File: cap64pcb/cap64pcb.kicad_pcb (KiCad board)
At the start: 2 copper layers, 91.6 x 8 mm, 29 parts, among them J1 SM05B_SURS_TF, Q1 BSS138, Q2 BSS138, U1 MPR121QR2, U2 SPX3819M5-L-3-3

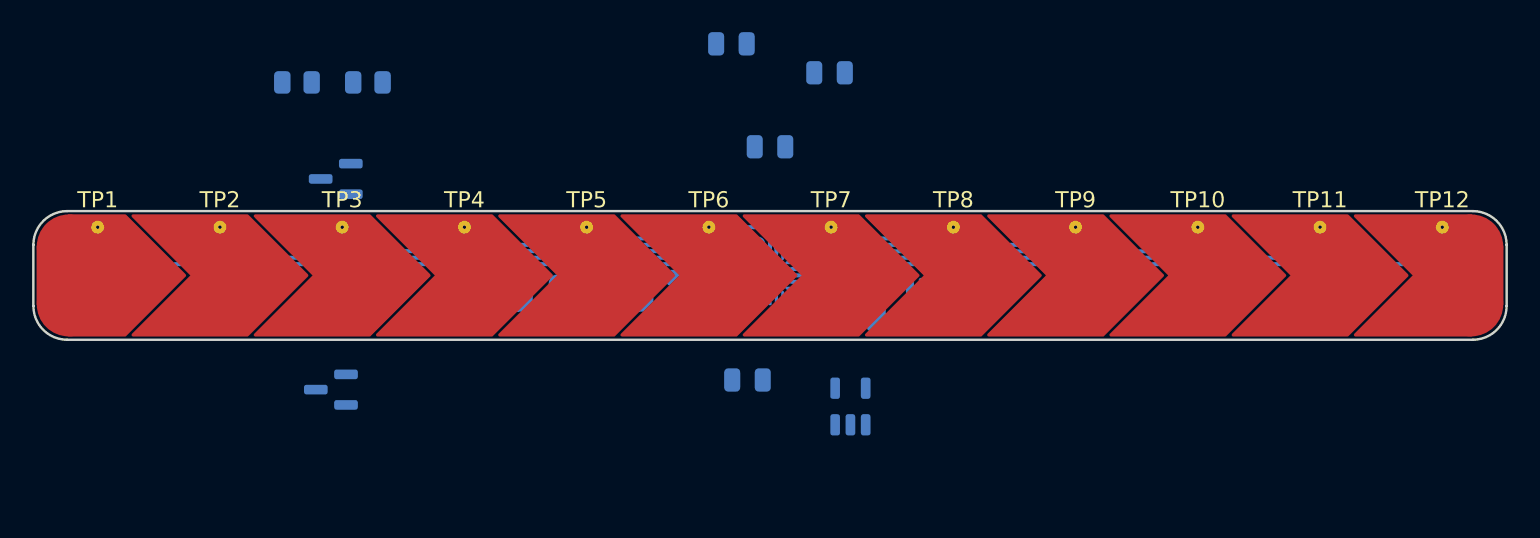
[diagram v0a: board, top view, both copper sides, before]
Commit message: updated sch and pcb with taller pads
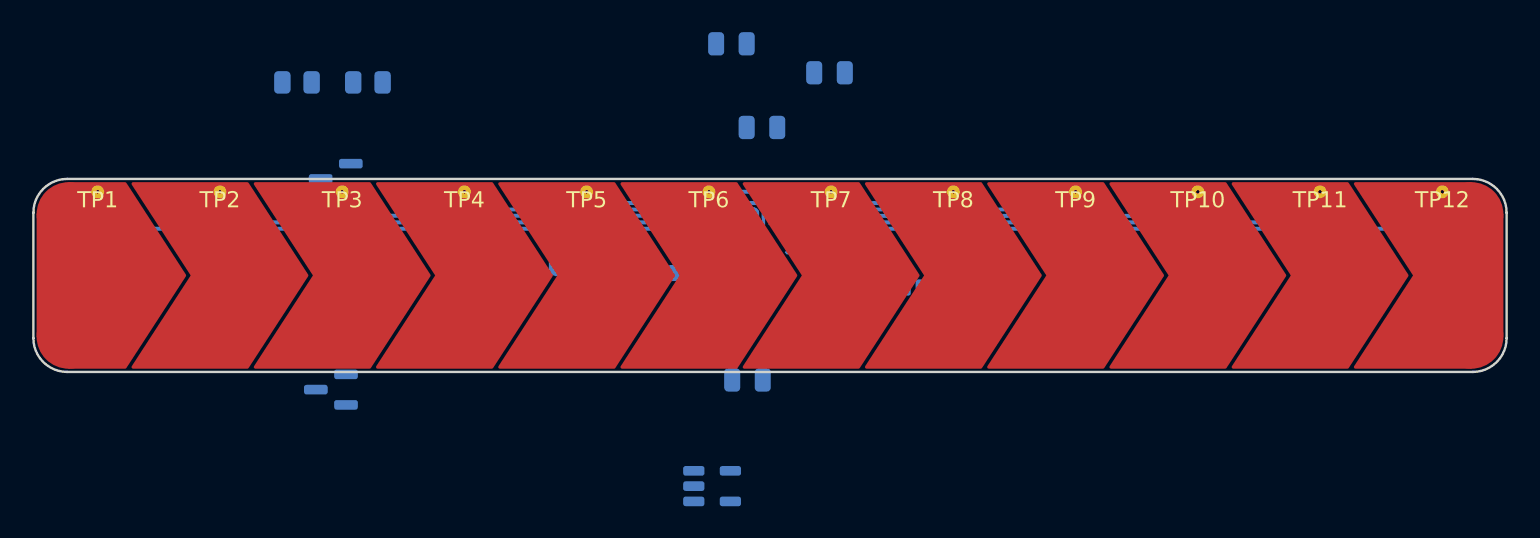
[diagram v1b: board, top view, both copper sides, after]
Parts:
- TP1: footprint cap_pads:CAPPAD_7.6x7.6_Chevron_1_TopPTH -> cap_pads:CAPPADS_7.6x11.6_Chevron_1
- TP10, TP11, TP2, TP3, TP4, TP5, TP6, TP7, TP8, TP9: footprint cap_pads:CAPPAD_7.6x7.6_Chevron_2_TopPTH -> cap_pads:CAPPADS_7.6x11.6_Chevron_2
- TP12: footprint cap_pads:CAPPAD_7.6x7.6_Chevron_3_TopPTH -> cap_pads:CAPPADS_7.6x11.6_Chevron_3
- moved U2 9.92 mm to (76.4, 58.1), turned to 0 degrees
- moved J1 2.42 mm to (88.5, 44.6), turned to 0 degrees
- moved C5 2.20 mm to (74.3, 43.9)
- moved JP1 2.20 mm to (69.5, 43.9)
- moved JP2 2.20 mm to (67.0, 43.9)
- moved JP3 2.20 mm to (64.5, 43.9)
- moved JP4 2.20 mm to (72.0, 43.9)
- moved R1 2.20 mm to (76.3, 43.9)
- moved U1 2.20 mm to (80.0, 42.8)
- moved C2 1.30 mm to (79.5, 35.8)
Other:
- board size 91.6 x 8 mm -> 91.6 x 12 mm

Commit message: shrunk pad radii by 0.01mm
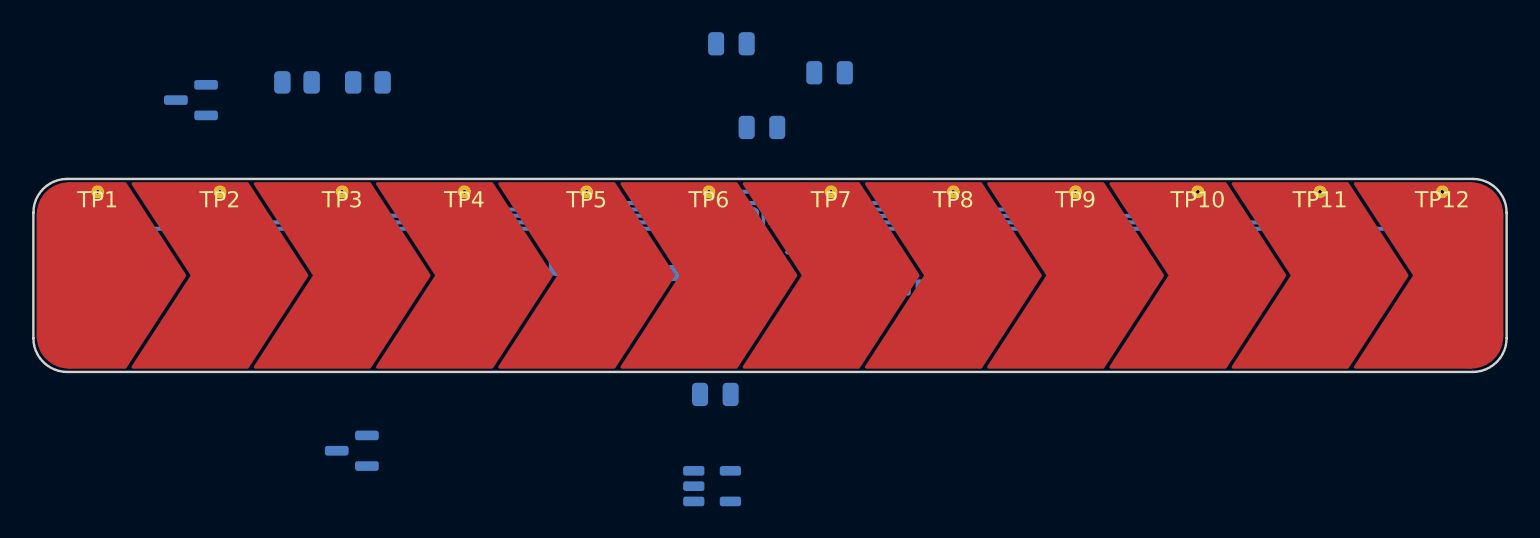
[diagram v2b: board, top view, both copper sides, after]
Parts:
- moved Q2 10.2 mm to (44.0, 34.1)
- moved Q1 4.02 mm to (54.0, 55.9)
- moved C4 2.19 mm to (76.6, 52.4)
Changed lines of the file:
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@@
             (xy -3.7 -3.8)
           ) (width 0.2) (fill yes))
-            (gr_circle (center -1.8 -3.8) (end 0.1 -3.8) (width 0.2) (fill yes))
-            (gr_circle (center -1.8 3.8) (end 0.1 3.8) (width 0.2) (fill yes))
+            (gr_circle (center -1.8 -3.8) (end 0.09 -3.8) (width 0.2) (fill yes))
+            (gr_circle (center -1.8 3.8) (end 0.09 3.8) (width 0.2) (fill yes))
       ))
     (pad "1" thru_hole circle (at 0 -5.2) (size 0.8 0.8) (drill 0.2) (layers *.Cu)
@@
             (xy -1.7 0)
           ) (width 0.2) (fill yes))
-            (gr_circle (center 1.8 3.8) (end 3.7 3.8) (width 0.2) (fill yes))
-            (gr_circle (center 1.8 -3.8) (end 3.7 -3.8) (width 0.2) (fill yes))
+            (gr_circle (center 1.8 3.8) (end 3.69 3.8) (width 0.2) (fill yes))
+            (gr_circle (center 1.8 -3.8) (end 3.69 -3.8) (width 0.2) (fill yes))
       ))
     (pad "1" thru_hole circle (at 0 -5.2) (size 0.8 0.8) (drill 0.2) (layers *.Cu)
@@
   )
   (footprint "Capacitor_SMD:C_0805_2012Metric" (layer "B.Cu")
-    (at 78.6 51.5 180)
+    (at 76.6 52.4 180)
     (descr "Capacitor SMD 0805 (2012 Metric), square (rectangular) end terminal, IPC_7351 nominal, (Body size source: IPC-SM-782 page 76, https://www.pcb-3d.com/wordpress/wp-content/uploads/ipc-sm-782a_amendment_1_and_2.pdf, https://docs.google.com/spreadsheets/d/1BsfQQcO9C6DZCsRaXUlFlo91Tg2WpOkGARC1WS5S8t0/edit?usp=sharing), generated with kicad-footprint-generator")
     (tags "capacitor")
@@
   )
   (footprint "Package_TO_SOT_SMD:SOT-23" (layer "B.Cu")
-    (at 52.7 52.1 180)
+    (at 54 55.9 180)
     (descr "SOT, 3 Pin (https://www.jedec.org/system/files/docs/to-236h.pdf variant AB), generated with kicad-footprint-generator ipc_gullwing_generator.py")
     (tags "SOT TO_SOT_SMD")
@@
   )
   (footprint "Package_TO_SOT_SMD:SOT-23" (layer "B.Cu")
-    (at 53 39 180)
+    (at 44 34.1 180)
     (descr "SOT, 3 Pin (https://www.jedec.org/system/files/docs/to-236h.pdf variant AB), generated with kicad-footprint-generator ipc_gullwing_generator.py")
     (tags "SOT TO_SOT_SMD")

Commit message: prepping silks
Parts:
- U2: value SPX3819M5-L-3-3 -> SPX3819M5-L-3.3
- moved C2 17.7 mm to (83.6, 53.0)
- moved JP1 15.0 mm to (62.8, 57.3), turned to -90 degrees
- moved JP3 13.1 mm to (71.0, 55.3), turned to -90 degrees
- moved JP2 12.5 mm to (67.4, 56.4), turned to -90 degrees
- moved U2 12.0 mm to (83.4, 48.3)
- moved C1 11.9 mm to (83.9, 44.3)
- moved JP4 1.70 mm to (70.3, 43.8)
- moved C5 1.70 mm to (72.6, 43.9)
- moved J1 1.26 mm to (89.7, 44.2)
- moved R1 1.06 mm to (75.6, 43.1), turned to 180 degrees
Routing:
- net GND: track 0.00 -> 9.16 mm

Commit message: arranging components
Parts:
- moved Q2 42.6 mm to (84.6, 47.0), turned to 0 degrees
- moved Q1 26.9 mm to (79.8, 48.4), turned to 0 degrees
- moved C1 7.92 mm to (91.0, 47.8)
- moved U2 7.65 mm to (90.7, 50.6), turned to 180 degrees
- moved J1 4.10 mm to (93.8, 44.1)
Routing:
- net Net-(TP12-Pad1): track 43.2 -> 42.2 mm
- net Net-(TP1-Pad1): track 43.0 -> 42.1 mm
- net Net-(TP11-Pad1): track 35.2 -> 34.4 mm
- net Net-(TP2-Pad1): track 35.0 -> 34.3 mm
- net Net-(TP10-Pad1): track 27.2 -> 26.6 mm
- net Net-(TP3-Pad1): track 27.0 -> 26.5 mm

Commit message: test traces
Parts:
- moved R2 34.7 mm to (83.2, 44.9), turned to -90 degrees
- moved R3 23.1 mm to (73.1, 47.4), turned to 90 degrees
- moved C3 18.0 mm to (77.3, 48.6), turned to -90 degrees
- moved JP1 10.6 mm to (68.1, 48.1), turned to 90 degrees
- moved JP2 9.68 mm to (70.7, 47.3), turned to 90 degrees
- moved JP3 8.32 mm to (79.3, 55.9), turned to 180 degrees
- moved C4 4.05 mm to (75.2, 48.6), turned to -90 degrees
- moved C2 3.72 mm to (85.8, 50.0)
- moved U2 2.20 mm to (89.6, 48.7)
- moved J1 2.15 mm to (95.8, 44.9)
- moved Q2 2.12 mm to (86.1, 45.5)
- moved C1 2.11 mm to (89.9, 46.0)
- moved Q1 1.03 mm to (80.3, 47.5)
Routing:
- net +3V3: track 0.00 -> 36.7 mm
- net GND: track 9.16 -> 45.8 mm
- net Net-(J1-Pad2): track 0.00 -> 19.0 mm
- net Net-(JP1-Pad2): track 0.00 -> 15.3 mm
- net Net-(J1-Pad3): track 0.00 -> 13.6 mm
- net SDA: track 0.00 -> 11.9 mm
- net Net-(C5-Pad1): track 0.00 -> 6.87 mm
- net SCL: track 0.00 -> 6.42 mm
- net VCC: track 0.00 -> 3.65 mm
- net Net-(C2-Pad1): track 0.00 -> 1.73 mm

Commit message: remove test traces
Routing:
- net GND: track 45.8 -> 0.00 mm
- net +3V3: track 36.7 -> 0.00 mm
- net Net-(J1-Pad2): track 19.0 -> 0.00 mm
- net Net-(JP1-Pad2): track 15.3 -> 0.00 mm
- net Net-(J1-Pad3): track 13.6 -> 0.00 mm
- net SDA: track 11.9 -> 0.00 mm
- net Net-(C5-Pad1): track 6.87 -> 0.00 mm
- net SCL: track 6.42 -> 0.00 mm
- net VCC: track 3.65 -> 0.00 mm
- net Net-(R1-Pad1): track 2.14 -> 0.00 mm
- net Net-(C2-Pad1): track 1.73 -> 0.00 mm
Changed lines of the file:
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@@
   (gr_line (start 36.3 39) (end 123.7 39) (layer "Edge.Cuts") (width 0.15))
   (gr_line (start 125.8 48.9) (end 125.8 41.1) (layer "Edge.Cuts") (width 0.15))
-  (segment (start 90.7375 48.05) (end 91.85 48.05) (width 0.25) (layer "B.Cu") (net 1))
-  (segment (start 91.85 49.136219) (end 91.036219 49.95) (width 0.25) (layer "B.Cu") (net 1))
-  (segment (start 91.85 48.05) (end 91.85 49.136219) (width 0.25) (layer "B.Cu") (net 1))
-  (segment (start 91.036219 49.95) (end 90.7375 49.95) (width 0.25) (layer "B.Cu") (net 1))
-  (segment (start 89.38952 48.48952) (end 89.9 49) (width 0.25) (layer "B.Cu") (net 2))
-  (segment (start 77.3 49.55) (end 75.2 49.55) (width 0.25) (layer "B.Cu") (net 2))
-  (segment (start 77.75625 43.6) (end 77.15625 44.2) (width 0.25) (layer "B.Cu") (net 2))
-  (segment (start 85.83952 49.01048) (end 84.85 50) (width 0.25) (layer "B.Cu") (net 2))
-  (segment (start 70.3 43.15) (end 70.35 43.1) (width 0.25) (layer "B.Cu") (net 2))
-  (segment (start 89.38952 48.48952) (end 88.86856 49.01048) (width 0.25) (layer "B.Cu") (net 2))
-  (segment (start 77.75 50) (end 77.3 49.55) (width 0.25) (layer "B.Cu") (net 2))
-  (segment (start 70.35 43.1) (end 72.45 43.1) (width 0.25) (layer "B.Cu") (net 2))
-  (segment (start 66.2 46.925912) (end 69.975912 43.15) (width 0.25) (layer "B.Cu") (net 2))
-  (segment (start 77.15625 44.2) (end 75.7875 44.2) (width 0.25) (layer "B.Cu") (net 2))
-  (segment (start 75.2 49.55) (end 74.55 50.2) (width 0.25) (layer "B.Cu") (net 2))
-  (segment (start 69.975912 43.15) (end 70.3 43.15) (width 0.25) (layer "B.Cu") (net 2))
-  (segment (start 74.55 50.2) (end 67.3 50.2) (width 0.25) (layer "B.Cu") (net 2))
-  (segment (start 74.6875 43.1) (end 72.75 43.1) (width 0.25) (layer "B.Cu") (net 2))
-  (segment (start 89.9 49) (end 90.7375 49) (width 0.25) (layer "B.Cu") (net 2))
-  (segment (start 72.45 43.1) (end 72.6 42.95) (width 0.25) (layer "B.Cu") (net 2))
-  (segment (start 89.38952 46.63952) (end 89.38952 48.48952) (width 0.25) (layer "B.Cu") (net 2))
-  (segment (start 66.2 49.1) (end 66.2 46.925912) (width 0.25) (layer "B.Cu") (net 2))
-  (segment (start 88.86856 49.01048) (end 85.83952 49.01048) (width 0.25) (layer "B.Cu") (net 2))
-  (segment (start 67.3 50.2) (end 66.2 49.1) (width 0.25) (layer "B.Cu") (net 2))
-  (segment (start 72.75 43.1) (end 72.6 42.95) (width 0.25) (layer "B.Cu") (net 2))
-  (segment (start 78.6125 43.6) (end 77.75625 43.6) (width 0.25) (layer "B.Cu") (net 2))
-  (segment (start 84.85 50) (end 77.75 50) (width 0.25) (layer "B.Cu") (net 2))
-  (segment (start 88.95 46.2) (end 89.38952 46.63952) (width 0.25) (layer "B.Cu") (net 2))
-  (segment (start 75.7875 44.2) (end 74.6875 43.1) (width 0.25) (layer "B.Cu") (net 2))
-  (segment (start 88.4625 49.95) (end 86.8 49.95) (width 0.25) (layer "B.Cu") (net 3))
-  (segment (start 86.8 49.95) (end 86.75 50) (width 0.25) (layer "B.Cu") (net 3))
-  (segment (start 73.7625 47.65) (end 73.1 48.3125) (width 0.25) (layer "B.Cu") (net 4))
-  (segment (start 85.1625 46.45) (end 84.35 46.45) (width 0.25) (layer "B.Cu") (net 4))
-  (segment (start 79.3625 48.45) (end 78.1 48.45) (width 0.25) (layer "B.Cu") (net 4))
-  (segment (start 83.1 43.6) (end 81.3875 43.6) (width 0.25) (layer "B.Cu") (net 4))
-  (segment (start 78.1 48.45) (end 77.3 47.65) (width 0.25) (layer "B.Cu") (net 4))
-  (segment (start 83.2 48.5) (end 79.4125 48.5) (width 0.25) (layer "B.Cu") (net 4))
-  (segment (start 84.35 46.45) (end 83.8 47) (width 0.25) (layer "B.Cu") (net 4))
-  (segment (start 83.8 47) (end 82.3 47) (width 0.25) (layer "B.Cu") (net 4))
-  (segment (start 79.3625 47.9375) (end 79.3625 48.45) (width 0.25) (layer "B.Cu") (net 4))
-  (segment (start 79.4125 48.5) (end 79.3625 48.45) (width 0.25) (layer "B.Cu") (net 4))
-  (segment (start 72.6625 48.75) (end 68.1 48.75) (width 0.25) (layer "B.Cu") (net 4))
-  (segment (start 86.16452 44.871699) (end 86.16452 44.228301) (width 0.25) (layer "B.Cu") (net 4))
-  (segment (start 83.2 43.9875) (end 83.2 43.7) (width 0.25) (layer "B.Cu") (net 4))
-  (segment (start 86.16452 44.228301) (end 85.536219 43.6) (width 0.25) (layer "B.Cu") (net 4))
-  (segment (start 83.2 43.7) (end 83.1 43.6) (width 0.25) (layer "B.Cu") (net 4))
-  (segment (start 77.3 47.65) (end 75.2 47.65) (width 0.25) (layer "B.Cu") (net 4))
-  (segment (start 85.536219 43.6) (end 83.1 43.6) (width 0.25) (layer "B.Cu") (net 4))
-  (segment (start 81.9 46.6) (end 80.7 46.6) (width 0.25) (layer "B.Cu") (net 4))
-  (segment (start 83.65 48.05) (end 83.2 48.5) (width 0.25) (layer "B.Cu") (net 4))
-  (segment (start 82.3 47) (end 81.9 46.6) (width 0.25) (layer "B.Cu") (net 4))
-  (segment (start 75.2 47.65) (end 73.7625 47.65) (width 0.25) (layer "B.Cu") (net 4))
-  (segment (start 88.4625 48.05) (end 83.65 48.05) (width 0.25) (layer "B.Cu") (net 4))
-  (segment (start 80.7 46.6) (end 79.3625 47.9375) (width 0.25) (layer "B.Cu") (net 4))
-  (segment (start 73.1 48.3125) (end 72.6625 48.75) (width 0.25) (layer "B.Cu") (net 4))
-  (segment (start 85.1625 45.873719) (end 86.16452 44.871699) (width 0.25) (layer "B.Cu") (net 4))
-  (segment (start 85.1625 46.45) (end 85.1625 45.873719) (width 0.25) (layer "B.Cu") (net 4))
-  (segment (start 78.5375 44.85) (end 72.6 44.85) (width 0.25) (layer "B.Cu") (net 5))
-  (segment (start 79.2 44.1875) (end 78.5375 44.85) (width 0.25) (layer "B.Cu") (net 5))
-  (segment (start 87.53548 46.06452) (end 86.1 47.5) (width 0.25) (layer "B.Cu") (net 6))
-  (segment (start 88.03952 45.821699) (end 87.796699 46.06452) (width 0.25) (layer "B.Cu") (net 6))
-  (segment (start 95 42.9) (end 90.7 42.9) (width 0.25) (layer "B.Cu") (net 6))
-  (segment (start 90.7 42.9) (end 88.03952 45.56048) (width 0.25) (layer "B.Cu") (net 6))
-  (segment (start 87.796699 46.06452) (end 87.53548 46.06452) (width 0.25) (layer "B.Cu") (net 6))
-  (segment (start 95 42.9) (end 95 46.05) (width 0.25) (layer "B.Cu") (net 6))
-  (segment (start 86.1 47.5) (end 81.2375 47.5) (width 0.25) (layer "B.Cu") (net 6))
-  (segment (start 88.03952 45.56048) (end 88.03952 45.821699) (width 0.25) (layer "B.Cu") (net 6))
-  (segment (start 95.8 42.5) (end 95.8 46.05) (width 0.25) (layer "B.Cu") (net 7))
-  (segment (start 90.0375 42.5) (end 87.0375 45.5) (width 0.25) (layer "B.Cu") (net 7))
-  (segment (start 95.8 42.5) (end 90.0375 42.5) (width 0.25) (layer "B.Cu") (net 7))
-  (segment (start 70.8 45.7) (end 70.7 45.6) (width 0.25) (layer "B.Cu") (net 9))
-  (segment (start 70.7 46.65) (end 70.7 45.6) (width 0.25) (layer "B.Cu") (net 9))
-  (segment (start 70.7 44.85) (end 70.3 44.45) (width 0.25) (layer "B.Cu") (net 9))
-  (segment (start 70.7 46.65) (end 68.9 46.65) (width 0.25) (layer "B.Cu") (net 9))
-  (segment (start 68.9 46.65) (end 68.1 47.45) (width 0.25) (layer "B.Cu") (net 9))
-  (segment (start 78.8 45.7) (end 70.8 45.7) (width 0.25) (layer "B.Cu") (net 9))
-  (segment (start 79.6 44.9) (end 78.8 45.7) (width 0.25) (layer "B.Cu") (net 9))
-  (segment (start 70.7 45.6) (end 70.7 44.85) (width 0.25) (layer "B.Cu") (net 9))
-  (segment (start 79.6 44.1875) (end 79.6 44.9) (width 0.25) (layer "B.Cu") (net 9))
-  (segment (start 79.3625 46.55) (end 73.1625 46.55) (width 0.25) (layer "B.Cu") (net 10))
-  (segment (start 80 45.9125) (end 79.3625 46.55) (width 0.25) (layer "B.Cu") (net 10))
-  (segment (start 73.1 46.4875) (end 71.6375 47.95) (width 0.25) (layer "B.Cu") (net 10))
-  (segment (start 73.1625 46.55) (end 73.1 46.4875) (width 0.25) (layer "B.Cu") (net 10))
-  (segment (start 71.6375 47.95) (end 70.7 47.95) (width 0.25) (layer "B.Cu") (net 10))
-  (segment (start 80 44.1875) (end 80 45.9125) (width 0.25) (layer "B.Cu") (net 10))
-  (segment (start 83.18548 44.91452) (end 84.79798 44.91452) (width 0.25) (layer "B.Cu") (net 11))
-  (segment (start 83.2 44.92904) (end 83.18548 44.91452) (width 0.25) (layer "B.Cu") (net 11))
-  (segment (start 84.79798 44.91452) (end 85.1625 44.55) (width 0.25) (layer "B.Cu") (net 11))
-  (segment (start 83.2 45.8125) (end 83.2 44.92904) (width 0.25) (layer "B.Cu") (net 11))
-  (segment (start 80.4 44.1875) (end 80.4 44.700656) (width 0.25) (layer "B.Cu") (net 11))
-  (segment (start 80.4 44.700656) (end 80.613864 44.91452) (width 0.25) (layer "B.Cu") (net 11))
-  (segment (start 80.613864 44.91452) (end 83.18548 44.91452) (width 0.25) (layer "B.Cu") (net 11))
-  (segment (start 78.6125 43.2) (end 76.6125 43.2) (width 0.25) (layer "B.Cu") (net 12))
-  (segment (start 76.6125 43.2) (end 76.5125 43.1) (width 0.25) (layer "B.Cu") (net 12))
   (segment (start 38.2 40.3) (end 38.2 39.8) (width 0.25) (layer "B.Cu") (net 13))
   (segment (start 76.834315 42.1) (end 40 42.1) (width 0.25) (layer "B.Cu") (net 13))

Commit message: update pcb
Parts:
- added D1: RED, LED_SMD:LED_0805_2012Metric, B.Cu at (85.7, 56.9)
- added R4: 10kΩ, Resistor_SMD:R_0805_2012Metric, B.Cu at (90.1, 56.9)
- J1: footprint Connector_JST:JST_SUR_SM05B-SURS-TF_1x05-1MP_P0.80mm_Horizontal -> Connector_JST:JST_SUR_SM04B-SURS-TF_1x04-1MP_P0.80mm_Horizontal
- U2: value SPX3819M5-L-3.3 -> SPX3819M5-L-3-3
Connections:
- J1 pad 4: INT -> GND
- U1 pad 1: INT -> Net-(U1-Pad1)
